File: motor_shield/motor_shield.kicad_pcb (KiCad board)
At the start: 2 copper layers, 61 x 52 mm, 22 parts, among them J1 Screw_Terminal_01x02, J2 Screw_Terminal_01x02, J3 Screw_Terminal_01x02, J4 Conn_01x04, J5 Conn_01x04, J6 Conn_01x04, U1 DRV8834_CARRIER, U10 SHARP_GP2Y0A21YK0F, U11 SHARP_GP2Y0A21YK0F, U2 DRV8834_CARRIER, U3 DRV8834_CARRIER, U4 ARDUINO_MICRO, U5 RASPBERRY_PI, U6 SHARP_GP2Y0A21YK0F, U7 SHARP_GP2Y0A21YK0F, U8 SHARP_GP2Y0A21YK0F, U9 SHARP_GP2Y0A21YK0F

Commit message: Continued work on motor shield
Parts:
- removed U11: SHARP_GP2Y0A21YK0F, Connector_JST:JST_XH_B03B-XH-A_1x03_P2.50mm_Vertical
- added C6: CP1_Small, Capacitor_THT:CP_Radial_D5.0mm_P2.50mm, F.Cu at (102.7, 91.1)
- added J7: Raspberry_Pi_2_3, Connector_PinHeader_2.54mm:PinHeader_2x20_P2.54mm_Vertical, F.Cu at (51.1, 50.5)
- C1: value CP1 -> CP3
- C2: value CP2 -> CP1
- C3: value CP3 -> CP2
- C4: value CP1 -> CP1_Small; footprint Capacitor_THT:CP_Radial_D8.0mm_P2.50mm -> Capacitor_THT:CP_Radial_D5.0mm_P2.50mm
- J1: value Screw_Terminal_01x02 -> MOTOR
- J2, J3: value Screw_Terminal_01x02 -> Conn_01x04; footprint CATPOO:TerminalBlock_Pololu-2_P5.00mm -> Connector_JST:JST_XH_B04B-XH-A_1x04_P2.50mm_Vertical
- J5: value Conn_01x04 -> ARDUINO; footprint Connector_JST:JST_XH_B04B-XH-A_1x04_P2.50mm_Vertical -> CATPOO:TerminalBlock_Pololu-2_P5.00mm
- J6: value Conn_01x04 -> RPI; footprint Connector_JST:JST_XH_B04B-XH-A_1x04_P2.50mm_Vertical -> CATPOO:TerminalBlock_Pololu-2_P5.00mm
- U5: value RASPBERRY_PI -> SHARP_GP2Y0A21YK0F; footprint Connector_PinHeader_2.54mm:PinHeader_2x20_P2.54mm_Vertical -> Connector_JST:JST_XH_B03B-XH-A_1x03_P2.50mm_Vertical
- moved J3 267.7 mm to (37.3, 109.0), turned to 90 degrees
- moved C5 265.6 mm to (39.9, 55.1), turned to 270 degrees
- moved J2 253.4 mm to (37.3, 91.2), turned to 90 degrees
- moved U10 208.0 mm to (102.7, 60.0)
- moved J6 206.4 mm to (38.4, 67.3), turned to 270 degrees
- moved U6 203.3 mm to (102.7, 112.0)
- moved U9 202.9 mm to (102.7, 70.1)
- moved J4 201.0 mm to (37.1, 126.7)
- moved U7 200.0 mm to (102.7, 101.2)
- moved U8 199.0 mm to (102.7, 80.3)
- moved J1 195.4 mm to (72.1, 128.8)
- moved C1 193.0 mm to (54.9, 75.9)
- moved C3 192.9 mm to (54.9, 129.3)
- moved C2 192.8 mm to (54.9, 102.6)
- moved U1 192.3 mm to (57.4, 69.6)
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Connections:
- net Net-(U4-Pad24) renamed /SIG4
- C4 pad 1: RPI_VIN -> ARDUINO_VIN
- C4 pad 2: RPI_GND -> ARDUINO_GND
- C5 pad 1: Net-(C5-Pad1) -> RPI_VIN
- C5 pad 2: ARDUINO_GND -> RPI_GND
- J2 pad 1: ARDUINO_VIN -> Net-(J2-Pad1)
- J2 pad 2: ARDUINO_GND -> Net-(J2-Pad2)
- J3 pad 1: RPI_VIN -> Net-(J3-Pad1)
- J3 pad 2: RPI_GND -> Net-(J3-Pad2)
- J5 pad 1: Net-(J5-Pad1) -> ARDUINO_VIN
- J5 pad 2: Net-(J5-Pad2) -> ARDUINO_GND
- J6 pad 1: Net-(J6-Pad1) -> RPI_VIN
- J6 pad 2: Net-(J6-Pad2) -> RPI_GND
- U1 pad 11: Net-(J4-Pad4) -> Net-(J2-Pad4)
- U1 pad 12: Net-(J4-Pad3) -> Net-(J2-Pad3)
- U1 pad 13: Net-(J4-Pad2) -> Net-(J2-Pad2)
- U1 pad 14: Net-(J4-Pad1) -> Net-(J2-Pad1)
- U1 pad 6: Net-(U1-Pad6) -> /SLEEP1
- U1 pad 7: Net-(U1-Pad7) -> /STEP1
- U1 pad 8: Net-(U1-Pad8) -> /DIR1
- U1 pad 9: GND -> ARDUINO_GND
- U10 pad 1: Net-(C5-Pad1) -> /5V
- U10 pad 2: ARDUINO_GND -> /GND
- U10 pad 3: Net-(U10-Pad3) -> /SIG6
- U2 pad 11: Net-(J5-Pad4) -> Net-(J3-Pad4)
- U2 pad 12: Net-(J5-Pad3) -> Net-(J3-Pad3)
- U2 pad 13: Net-(J5-Pad2) -> Net-(J3-Pad2)
- U2 pad 14: Net-(J5-Pad1) -> Net-(J3-Pad1)
- U2 pad 6: Net-(U2-Pad6) -> /SLEEP2
- U2 pad 7: Net-(U2-Pad7) -> /STEP2
- U2 pad 8: Net-(U2-Pad8) -> /DIR2
- U2 pad 9: GND -> ARDUINO_GND
- U3 pad 11: Net-(J6-Pad4) -> Net-(J4-Pad4)
- U3 pad 12: Net-(J6-Pad3) -> Net-(J4-Pad3)
- U3 pad 13: Net-(J6-Pad2) -> Net-(J4-Pad2)
- U3 pad 14: Net-(J6-Pad1) -> Net-(J4-Pad1)
- U3 pad 6: Net-(U3-Pad6) -> /SLEEP3
- U3 pad 7: Net-(U3-Pad7) -> /STEP3
- U3 pad 8: Net-(U3-Pad8) -> /DIR3
- U3 pad 9: GND -> ARDUINO_GND
- U4 pad 10: Net-(U1-Pad7) -> /SLEEP1
- U4 pad 11: Net-(U1-Pad8) -> /STEP1
- U4 pad 12: Net-(U2-Pad6) -> /DIR1
- U4 pad 13: Net-(U2-Pad7) -> /SLEEP2
- U4 pad 14: Net-(U2-Pad8) -> /STEP2
- U4 pad 15: Net-(U3-Pad6) -> /DIR2
- U4 pad 16: Net-(U3-Pad7) -> /SLEEP3
- U4 pad 17: Net-(U3-Pad8) -> /STEP3
- U4 pad 18: (no net) -> /DIR3
- U4 pad 21: Net-(U11-Pad3) -> /SIG1
- U4 pad 22: Net-(U10-Pad3) -> /SIG2
- U4 pad 23: Net-(U4-Pad23) -> /SIG3
- U4 pad 25: Net-(U4-Pad25) -> /SIG5
- U4 pad 26: Net-(U4-Pad26) -> /SIG6
- U4 pad 29: Net-(C5-Pad1) -> (no net)
- U4 pad 31: ARDUINO_GND -> (no net)
- U4 pad 6: (no net) -> ARDUINO_GND
- U4 pad 7: Net-(U4-Pad7) -> Net-(J7-Pad3)
- U4 pad 8: Net-(U4-Pad8) -> Net-(J7-Pad5)
- U4 pad 9: Net-(U1-Pad6) -> (no net)
- U5 pad 1: (no net) -> /5V
- U5 pad 2: (no net) -> /GND
- U5 pad 3: Net-(U4-Pad7) -> /SIG1
- U6 pad 1: Net-(C5-Pad1) -> /5V
- U6 pad 2: ARDUINO_GND -> /GND
- U6 pad 3: Net-(U4-Pad26) -> /SIG2
- U7 pad 1: Net-(C5-Pad1) -> /5V
- U7 pad 2: ARDUINO_GND -> /GND
- U7 pad 3: Net-(U4-Pad25) -> /SIG3
- U8 pad 1: Net-(C5-Pad1) -> /5V
- U8 pad 2: ARDUINO_GND -> /GND
- U9 pad 1: Net-(C5-Pad1) -> /5V
- U9 pad 2: ARDUINO_GND -> /GND
- U9 pad 3: Net-(U4-Pad23) -> /SIG5
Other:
- board size 61 x 52 mm -> 85 x 95 mm

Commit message: Finish circuit board design
off to oshpark!
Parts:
- removed J1: MOTOR, CATPOO:TerminalBlock_Pololu-2_P5.00mm
- added D1: 1N4001, Diode_THT:D_DO-41_SOD81_P10.16mm_Horizontal, F.Cu at (91.4, 120.9)
- J5: value ARDUINO -> MOTOR PWR
- J6: value RPI -> RPI PWR
- moved C4 24.7 mm to (82.3, 58.4), turned to 0 degrees
- moved C5 18.6 mm to (38.4, 73.7), turned to 90 degrees
- moved J5 12.8 mm to (74.2, 131.1)
- moved J6 11.7 mm to (38.4, 55.6)
- moved C1 4.32 mm to (59.2, 75.9), turned to 180 degrees
- moved C2 4.32 mm to (59.2, 102.6), turned to 180 degrees
- moved C3 4.32 mm to (59.2, 129.3), turned to 180 degrees
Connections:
- net Net-(J7-Pad3) renamed /SDA
- net Net-(J7-Pad5) renamed /SCL
- C4 pad 1: ARDUINO_VIN -> Net-(C4-Pad1)
- C4 pad 2: ARDUINO_GND -> MOTOR_GND
- C6 pad 2: /GND -> MOTOR_GND
- J5 pad 1: ARDUINO_VIN -> MOTOR_VIN
- J5 pad 2: ARDUINO_GND -> MOTOR_GND
- U10 pad 2: /GND -> MOTOR_GND
- U4 pad 10: /SLEEP1 -> /DIR1
- U4 pad 12: /DIR1 -> /SLEEP1
- U4 pad 13: /SLEEP2 -> /DIR2
- U4 pad 15: /DIR2 -> /SLEEP2
- U4 pad 16: /SLEEP3 -> /DIR3
- U4 pad 18: /DIR3 -> /SLEEP3
- U4 pad 29: (no net) -> /5V
- U4 pad 31: (no net) -> MOTOR_GND
- U4 pad 32: ARDUINO_VIN -> Net-(C4-Pad1)
- U4 pad 6: ARDUINO_GND -> (no net)
- U5 pad 2: /GND -> MOTOR_GND
- U6 pad 2: /GND -> MOTOR_GND
- U7 pad 2: /GND -> MOTOR_GND
- U8 pad 2: /GND -> MOTOR_GND
- U9 pad 2: /GND -> MOTOR_GND
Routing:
- net MOTOR_GND: track 0.00 -> 327.5 mm
- net MOTOR_VIN: track 0.00 -> 133.2 mm
- net Net-(C4-Pad1): track 0.00 -> 93.6 mm
- net /5V: track 0.00 -> 84.4 mm
- net ARDUINO_GND: track 0.00 -> 58.9 mm
- net RPI_VIN: track 0.00 -> 53.8 mm
- net RPI_GND: track 0.00 -> 51.0 mm
- net /SCL: track 0.00 -> 46.7 mm
- net /SDA: track 0.00 -> 44.3 mm
- net /SIG6: track 0.00 -> 35.6 mm
- net /SLEEP1: track 0.00 -> 35.3 mm
- net /DIR1: track 0.00 -> 35.3 mm
- net /STEP1: track 0.00 -> 35.3 mm
- net /SLEEP3: track 0.00 -> 31.6 mm
- net /SIG1: track 0.00 -> 30.4 mm
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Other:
- net class Default: clearance 0.254 -> 0.25; trace_width 0.254 -> 0.635
- rule trace_clearance: 0.254 -> 0.25
- board text added: "5V"
- board text added: "9V"
- board text added: "github.com/timmd909/catpoo v5"

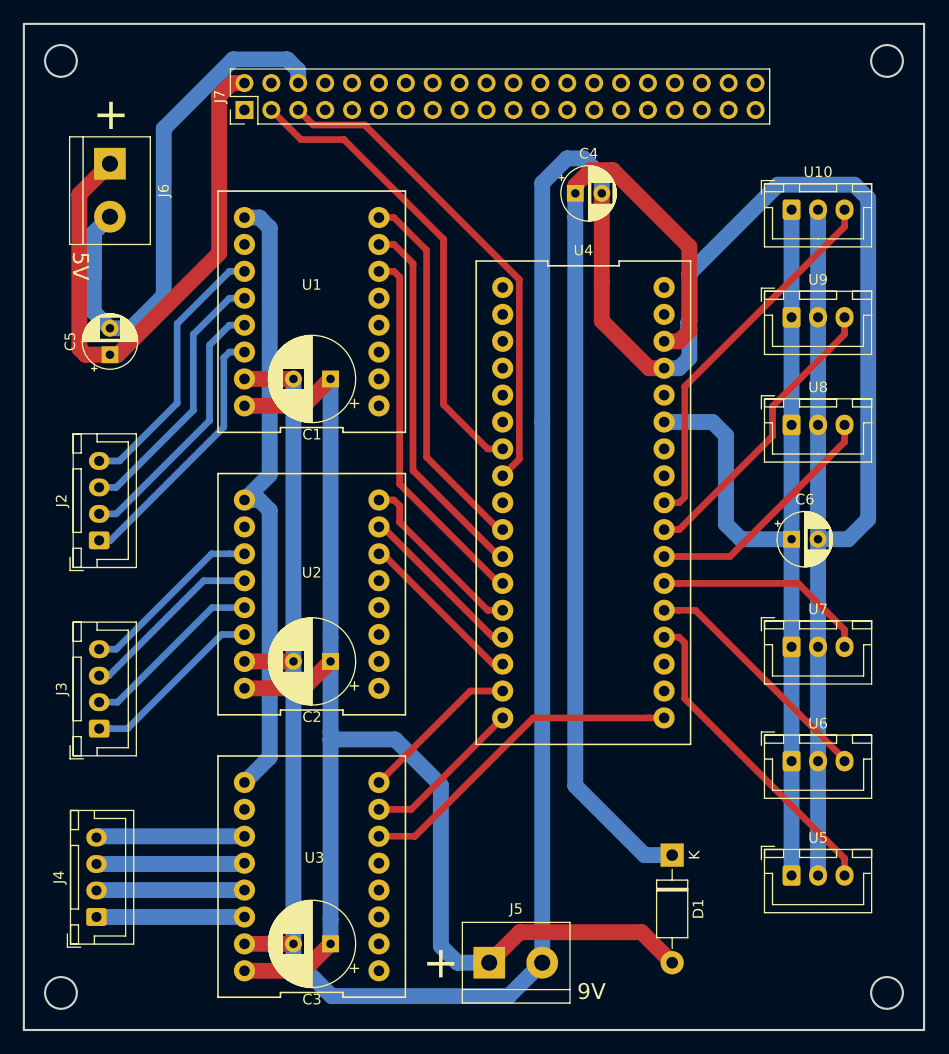
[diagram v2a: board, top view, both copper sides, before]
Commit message: Updated origin but no functional changes
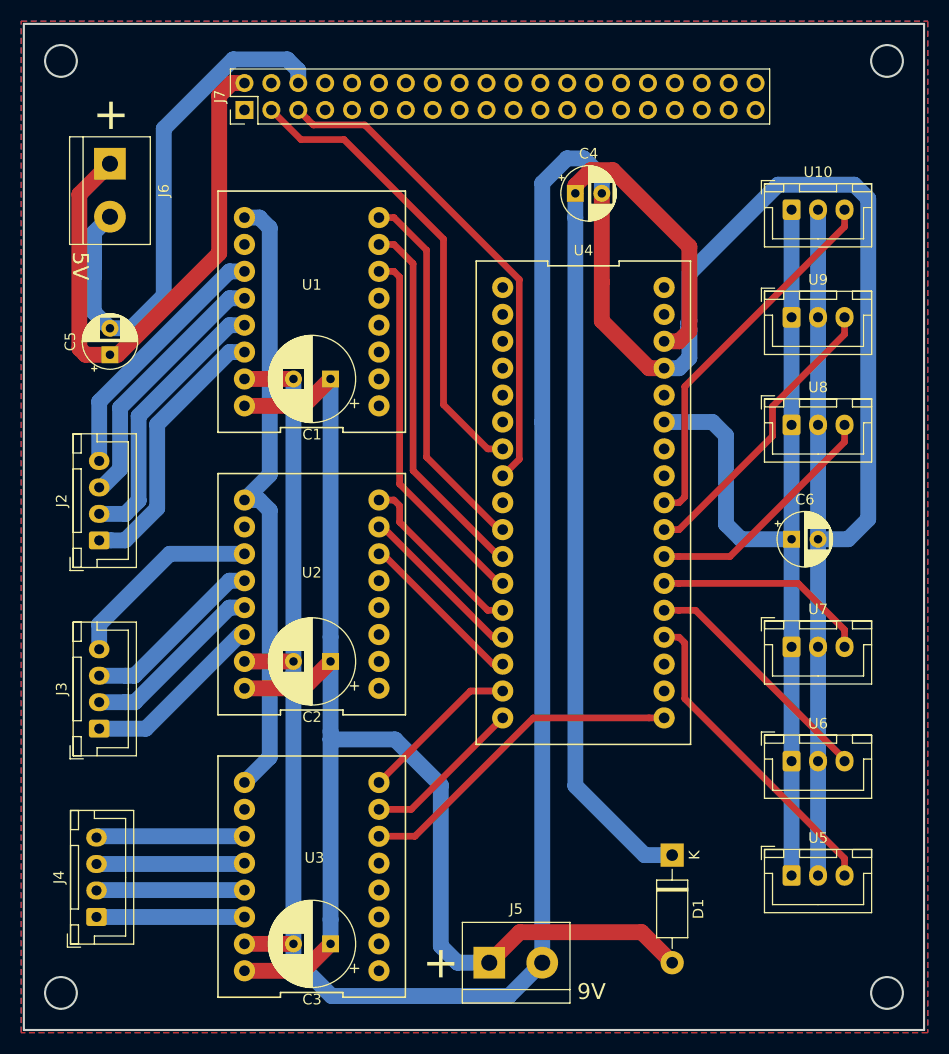
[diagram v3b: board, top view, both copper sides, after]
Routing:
- net Net-(J3-Pad4): track 17.4 -> 18.8 mm
- net Net-(J2-Pad4): track 25.5 -> 24.4 mm
- net Net-(J2-Pad1): track 24.9 -> 25.7 mm
- net Net-(J2-Pad3): track 25.3 -> 24.5 mm
- net Net-(J2-Pad2): track 25.3 -> 25.8 mm
- added copper zone on B.Cu, net MOTOR_GND
- added copper zone on F.Cu, net MOTOR_GND
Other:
- rule trace_min: 0.1524 -> 0.2

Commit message: Remove the RPI connector and power supply
The board for holding the Arduino was too complicated, and
didn't allow me to use the protoshield on the RPI. This
also is 33% less expensive to fabricate.
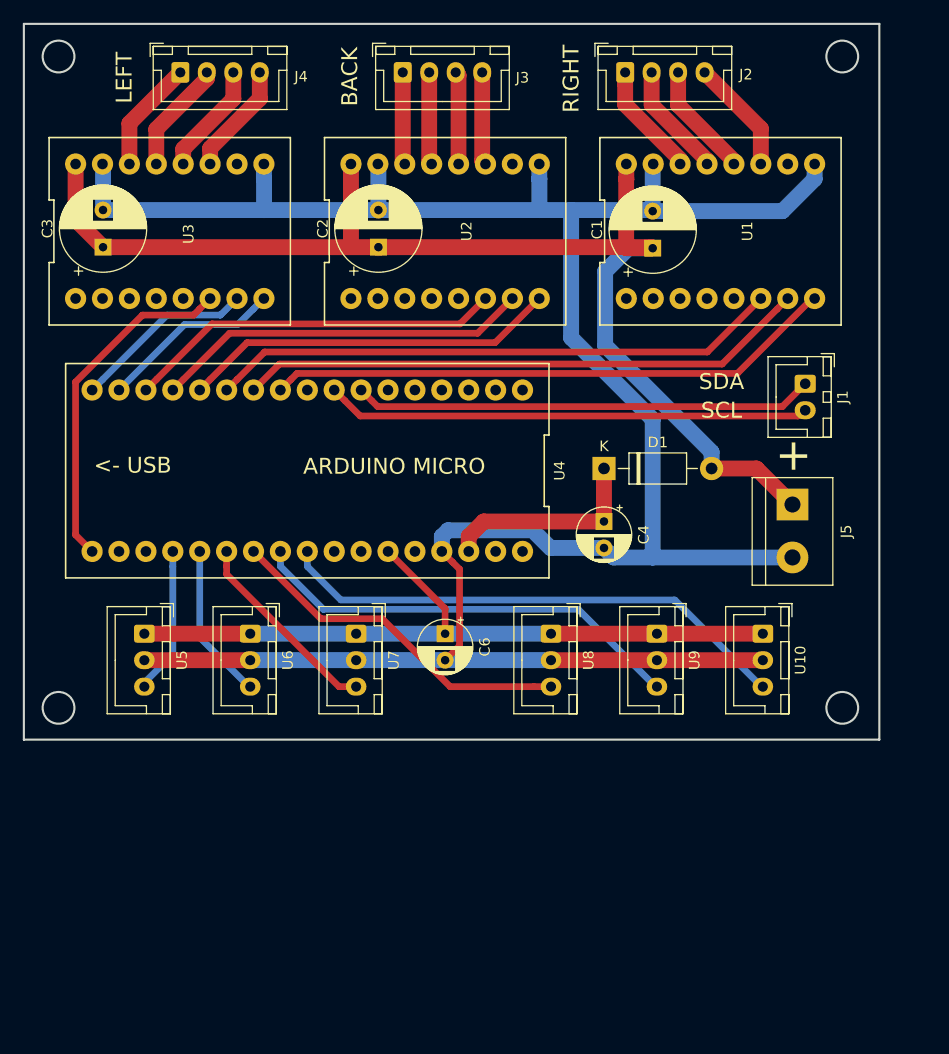
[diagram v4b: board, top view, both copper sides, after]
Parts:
- removed C5: CP1_Small, Capacitor_THT:CP_Radial_D5.0mm_P2.50mm
- removed J6: RPI PWR, CATPOO:TerminalBlock_Pololu-2_P5.00mm
- removed J7: Raspberry_Pi_2_3, Connector_PinHeader_2.54mm:PinHeader_2x20_P2.54mm_Vertical
- added J1: Conn_01x02, Connector_JST:JST_XH_B02B-XH-A_1x02_P2.50mm_Vertical, F.Cu at (104.0, 76.4)
- moved J4 80.1 mm to (45.0, 47.0), turned to 0 degrees
- moved C3 69.2 mm to (37.7, 63.5), turned to 90 degrees
- moved J3 68.3 mm to (66.0, 47.0), turned to 0 degrees
- moved J2 66.5 mm to (87.0, 47.0), turned to 0 degrees
- moved U5 65.2 mm to (41.6, 100.0), turned to 270 degrees
- moved U3 62.4 mm to (44.0, 62.0), turned to 0 degrees
- moved U6 52.5 mm to (51.6, 100.0), turned to 270 degrees
- moved J5 51.9 mm to (102.8, 87.8), turned to 270 degrees
- moved U7 41.1 mm to (61.6, 100.0), turned to 270 degrees
- moved U10 40.1 mm to (100.0, 100.0), turned to 270 degrees
- moved C2 39.4 mm to (63.7, 63.5), turned to 90 degrees
- moved U1 39.3 mm to (96.0, 62.0), turned to 0 degrees
- moved D1 37.1 mm to (85.0, 84.4), turned to 0 degrees
- moved U2 36.5 mm to (70.0, 62.0), turned to 0 degrees
- moved C6 33.9 mm to (70.0, 100.0), turned to 270 degrees
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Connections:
- U1 pad 9: ARDUINO_GND -> MOTOR_GND
- U2 pad 9: ARDUINO_GND -> MOTOR_GND
- U3 pad 9: ARDUINO_GND -> MOTOR_GND
- U4 pad 7: /SDA -> Net-(J1-Pad1)
- U4 pad 8: /SCL -> Net-(J1-Pad2)
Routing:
- net MOTOR_GND: track 327.5 -> 233.6 mm
- net Net-(C4-Pad1): track 93.6 -> 19.8 mm
- net ARDUINO_GND: track 58.9 -> 0.00 mm
- net RPI_VIN: track 53.8 -> 0.00 mm
- net RPI_GND: track 51.0 -> 0.00 mm
- net /SCL: track 46.7 -> 0.00 mm
- net Net-(J1-Pad2): track 0.00 -> 45.7 mm
- net /SDA: track 44.3 -> 0.00 mm
- net Net-(J1-Pad1): track 0.00 -> 43.5 mm
- net /SLEEP2: track 16.0 -> 35.6 mm
- net /STEP2: track 16.0 -> 35.6 mm
- net /DIR2: track 16.9 -> 35.6 mm
- net /SLEEP1: track 35.3 -> 54.0 mm
- net /DIR1: track 35.3 -> 54.0 mm
- net /STEP1: track 35.3 -> 54.0 mm
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- removed copper zone on B.Cu, net MOTOR_GND
- removed copper zone on F.Cu, net MOTOR_GND
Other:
- board size 85 x 95 mm -> 80.8 x 67.6 mm
- board text added: "<- USB"
- board text added: "ARDUINO MICRO"
- board text added: "BACK"
- board text added: "LEFT"
- board text added: "RIGHT"
- board text added: "SCL"
- board text added: "SDA"
- board text added: "github.com/timmd909/catpoo v6"
- board text removed: "5V"
- board text removed: "9V"
- board text removed: "github.com/timmd909/catpoo v5"
